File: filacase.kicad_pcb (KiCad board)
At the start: 2 copper layers, 86 x 50 mm, 42 parts, among them J1 Expansion_2, J2 SDcard, J3 SPI 1, J4 Expansion_1, J5 SPI 2, J6 Serial TAG, J7 I2C, J8 +5V, J9 dbg/download port, M3 MountingHole_2.2mm_M2_Pad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

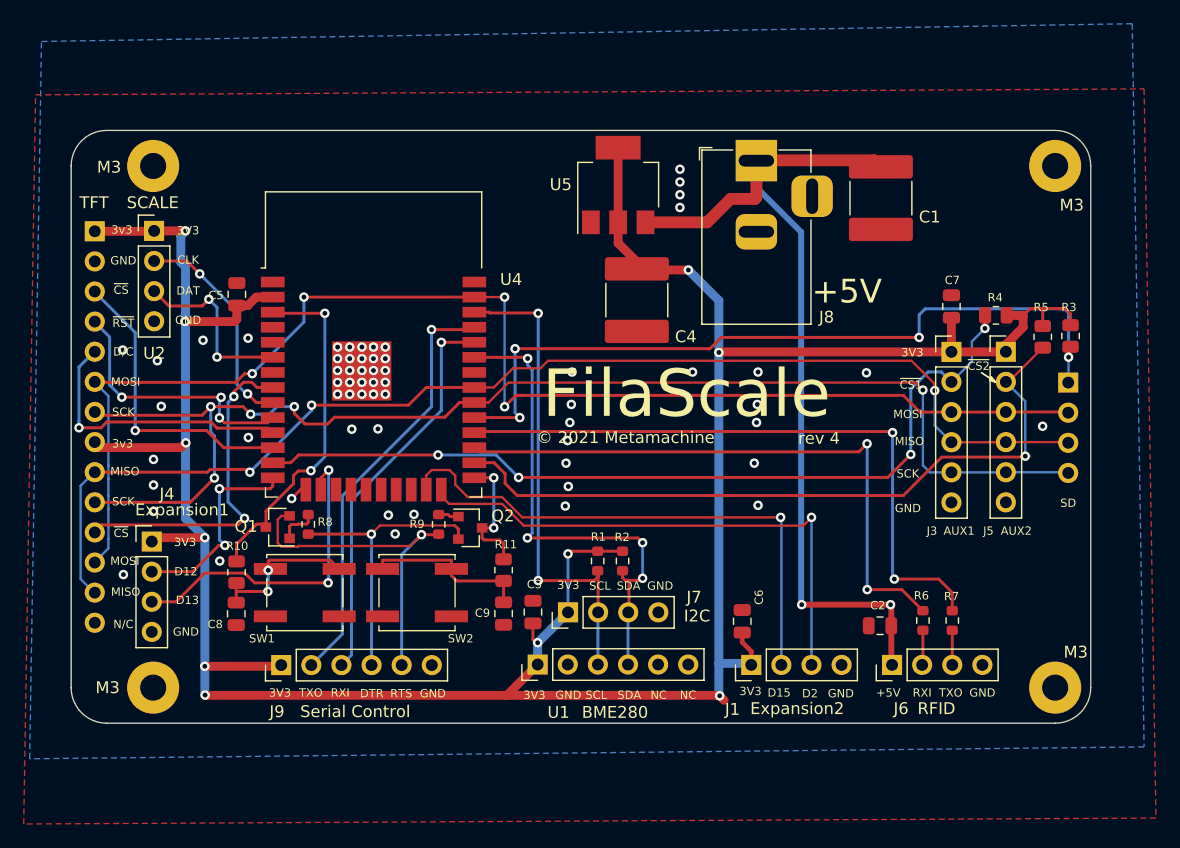
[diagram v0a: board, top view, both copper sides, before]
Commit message: Flip TFT connector around the right way
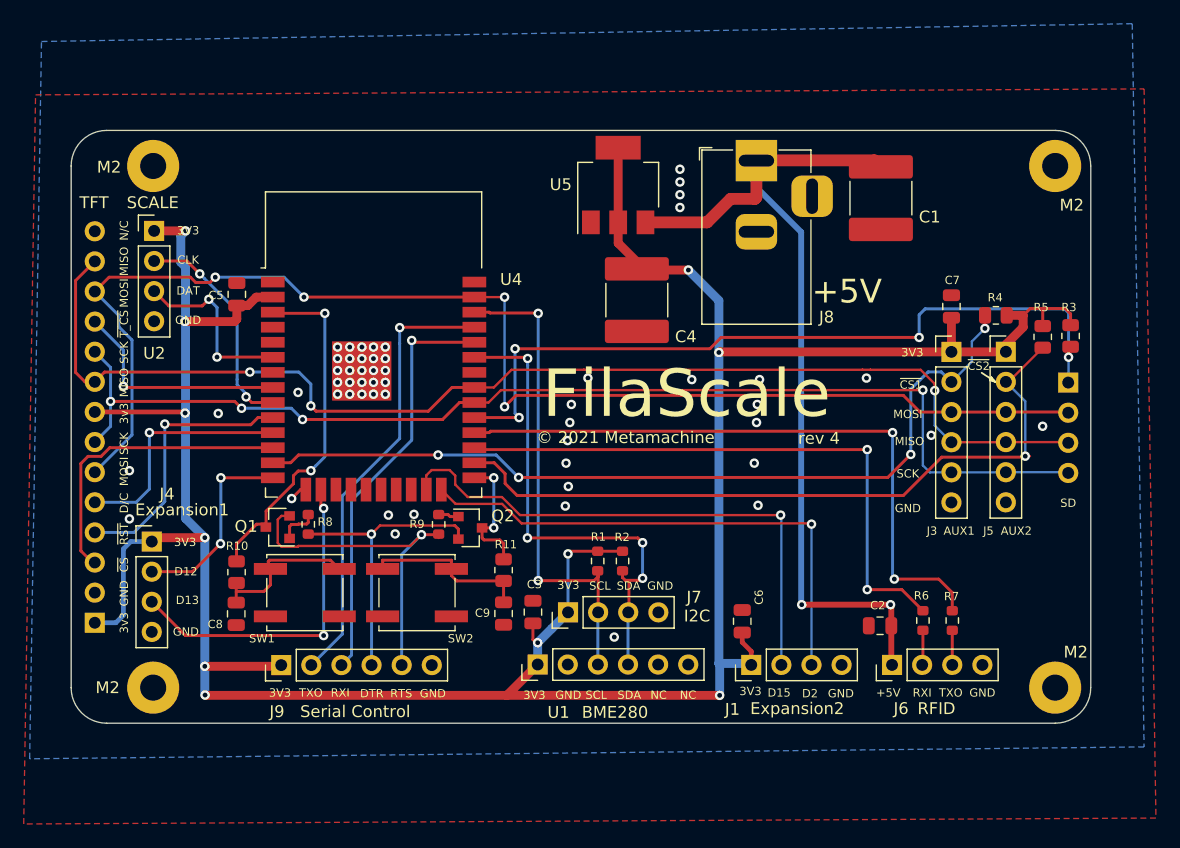
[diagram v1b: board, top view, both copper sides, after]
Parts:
- removed M3 (x2): MountingHole_2.2mm_M2_Pad, MountingHole:MountingHole_2.2mm_M2_Pad
- added M2: MountingHole_2.2mm_M2_Pad, MountingHole:MountingHole_2.2mm_M2_Pad, F.Cu at (64.9, 94.0)
- added M2: MountingHole_2.2mm_M2_Pad, MountingHole:MountingHole_2.2mm_M2_Pad, F.Cu at (141.0, 94.0)
- moved U3 33.0 mm to (60.0, 132.5), turned to 0 degrees
- renumbered M3 to M2
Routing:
- net /SPI_SCK: track 109.5 -> 97.8 mm, vias 5 -> 4
- net /~T_CS~: track 28.4 -> 19.1 mm, vias 2 -> 1
- net +3V3: track 238.2 -> 243.5 mm
- net /TFT_DC: track 23.9 -> 20.2 mm
- net /RX_IN: track 33.5 -> 35.2 mm
- net /TX_OUT: track 36.2 -> 37.9 mm
- net /D2: track 45.5 -> 44.3 mm
- net /SPI_MOSI: track 112.9 -> 111.8 mm
- net /TAG_RX: track 51.3 -> 50.4 mm
- net /D12: track 17.4 -> 16.7 mm
- net /~TFT_RST~: track 22.4 -> 23.0 mm, vias 3 -> 1
- net /~TFT_CS~: track 25.4 -> 25.7 mm, vias 1 -> 0
- net Net-(C8-Pad1): vias 2 -> 0
- net GND: vias 61 -> 54
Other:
- board text added: "~T_CS~"

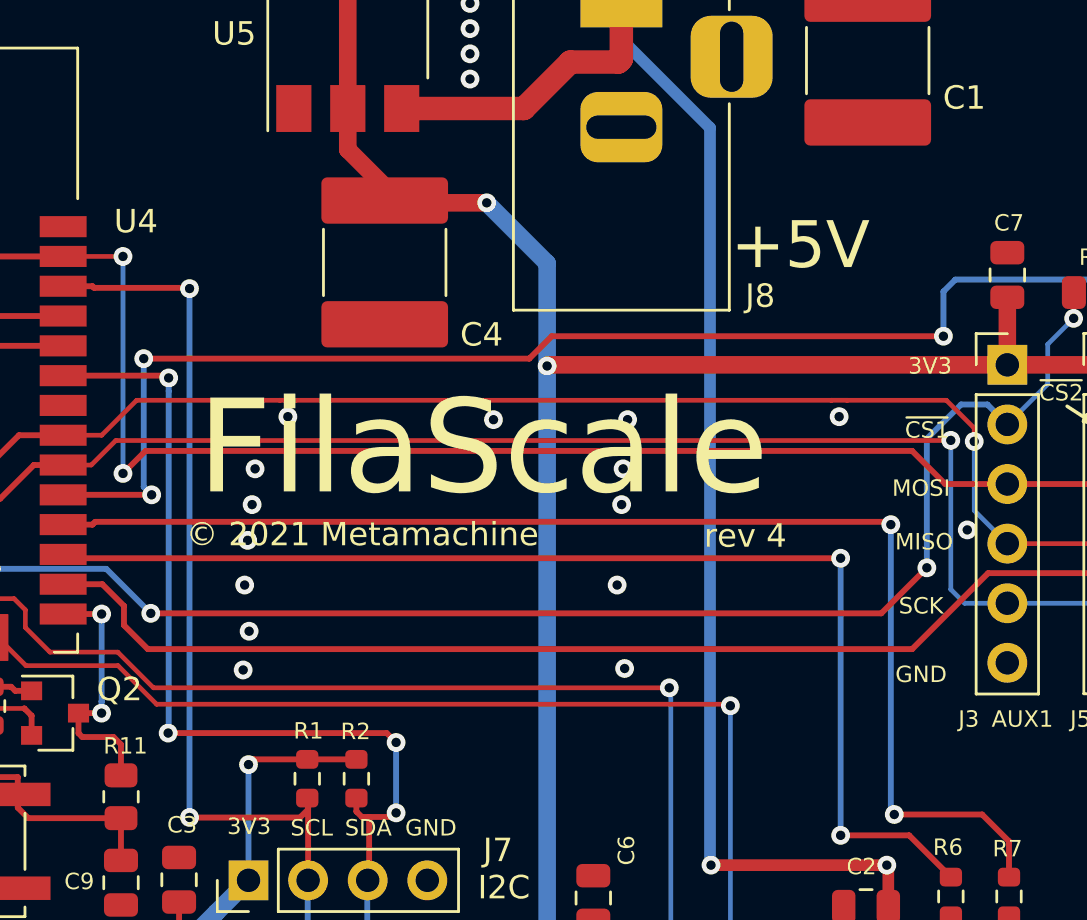
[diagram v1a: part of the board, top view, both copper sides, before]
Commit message: Tweak the layout of a couple of tracks
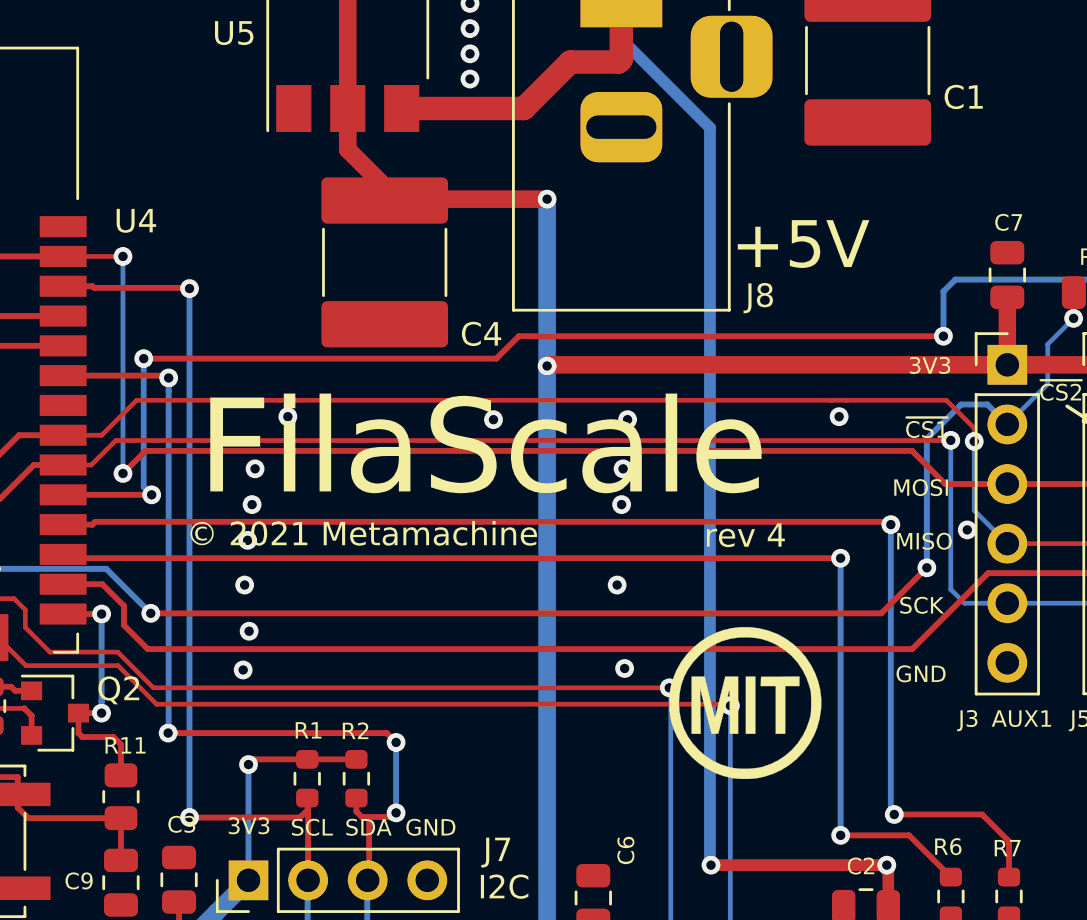
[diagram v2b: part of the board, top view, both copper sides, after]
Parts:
- added G***: LOGO, weo_footprints:MIT_Logo, F.Cu at (121.1, 124.1)
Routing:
- net +3V3: track 243.5 -> 245.1 mm
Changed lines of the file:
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@@
     (thickness 1.6)
     (drawings 85)
-    (tracks 555)
+    (tracks 554)
     (zones 0)
-    (modules 42)
+    (modules 43)
     (nets 50)
   )
@@
     (add_net "Net-(U4-Pad7)")
   )
+  (module weo_footprints:MIT_Logo (layer F.Cu)
+    (at 121.0815 124.0815)
+    (fp_text reference G*** (at 0 0) (layer F.SilkS) hide
+      (effects (font (size 1.524 1.524) (thickness 0.3)))
+    )
+    (fp_text value LOGO (at 0.75 0) (layer F.SilkS) hide
+      (effects (font (size 1.524 1.524) (thickness 0.3)))
+    )
+    (fp_poly (pts (xy 0.189754 -3.220101) (xy 0.581236 -3.173113) (xy 0.963959 -3.080709) (xy 1.331155 -2.943384)
+      (xy 1.400605 -2.911302) (xy 1.739175 -2.722743) (xy 2.049878 -2.495615) (xy 2.330249 -2.234253)
+      (xy 2.577827 -1.942993) (xy 2.790147 -1.626168) (xy 2.964747 -1.288115) (xy 3.099163 -0.93317)
+      (xy 3.190932 -0.565666) (xy 3.237591 -0.189939) (xy 3.236677 0.189675) (xy 3.226842 0.302874)
+      (xy 3.16401 0.700748) (xy 3.062539 1.069577) (xy 2.920238 1.415702) (xy 2.734915 1.745467)
+      (xy 2.720676 1.767485) (xy 2.476291 2.097344) (xy 2.19871 2.389917) (xy 1.890714 2.643367)
+      (xy 1.555087 2.855858) (xy 1.194611 3.025554) (xy 0.812068 3.150616) (xy 0.535274 3.21017)
+      (xy 0.34563 3.233438) (xy 0.125654 3.245624) (xy -0.105404 3.246702) (xy -0.328295 3.236649)
+      (xy -0.523769 3.215437) (xy -0.547697 3.211602) (xy -0.930196 3.121982) (xy -1.297572 2.985883)
+      (xy -1.645622 2.806436) (xy -1.970141 2.586776) (xy -2.266925 2.330034) (xy -2.53177 2.039345)
+      (xy -2.760473 1.71784) (xy -2.908969 1.451919) (xy -3.035932 1.170407) (xy -3.128962 0.899999)
+      (xy -3.191338 0.626325) (xy -3.226335 0.335017) (xy -3.237233 0.0127) (xy -2.825231 0.0127)
+      (xy -2.802632 0.395327) (xy -2.734462 0.755906) (xy -2.620161 1.095751) (xy -2.45917 1.416174)
+      (xy -2.250929 1.718488) (xy -1.99488 2.004007) (xy -1.964323 2.033913) (xy -1.674413 2.280209)
+      (xy -1.360506 2.481731) (xy -1.022594 2.638482) (xy -0.660672 2.750465) (xy -0.5715 2.770418)
+      (xy -0.368461 2.800104) (xy -0.134216 2.813797) (xy 0.114382 2.811974) (xy 0.36048 2.79511)
+      (xy 0.587228 2.763682) (xy 0.723303 2.733831) (xy 1.076518 2.615069) (xy 1.406778 2.452648)
+      (xy 1.710981 2.249672) (xy 1.986025 2.00924) (xy 2.228809 1.734456) (xy 2.43623 1.428422)
+      (xy 2.605187 1.094238) (xy 2.732576 0.735007) (xy 2.736638 0.720608) (xy 2.762186 0.625487)
+      (xy 2.780667 0.543335) (xy 2.793211 0.462724) (xy 2.800949 0.372222) (xy 2.805014 0.260402)
+      (xy 2.806536 0.115832) (xy 2.8067 0.0127) (xy 2.806133 -0.156048) (xy 2.803677 -0.285431)
+      (xy 2.798203 -0.386879) (xy 2.788578 -0.471822) (xy 2.773672 -0.551689) (xy 2.752352 -0.63791)
+      (xy 2.736638 -0.695209) (xy 2.609156 -1.06164) (xy 2.440011 -1.400723) (xy 2.231151 -1.710099)
+      (xy 1.984523 -1.987407) (xy 1.702075 -2.230286) (xy 1.385754 -2.436376) (xy 1.23491 -2.515493)
+      (xy 0.978252 -2.627342) (xy 0.727007 -2.706851) (xy 0.464922 -2.757945) (xy 0.175748 -2.784549)
+      (xy 0.1089 -2.787433) (xy -0.282191 -2.778839) (xy -0.652037 -2.724159) (xy -1.001259 -2.623159)
+      (xy -1.330479 -2.475605) (xy -1.640316 -2.281265) (xy -1.931393 -2.039905) (xy -1.964323 -2.008514)
+      (xy -2.225572 -1.724731) (xy -2.438952 -1.424295) (xy -2.605023 -1.105893) (xy -2.724342 -0.76821)
+      (xy -2.797471 -0.409935) (xy -2.824968 -0.029754) (xy -2.825231 0.0127) (xy -3.237233 0.0127)
+      (xy -3.232483 -0.230688) (xy -3.2166 -0.440344) (xy -3.187129 -0.632591) (xy -3.141616 -0.823749)
+      (xy -3.082774 -1.01476) (xy -2.934783 -1.378837) (xy -2.743139 -1.721167) (xy -2.511704 -2.037966)
+      (xy -2.244342 -2.325453) (xy -1.944917 -2.579845) (xy -1.617292 -2.79736) (xy -1.26533 -2.974215)
+      (xy -0.96956 -3.083654) (xy -0.592412 -3.175864) (xy -0.203718 -3.221182) (xy 0.189754 -3.220101)) (layer F.SilkS) (width 0.01))
+    (fp_poly (pts (xy -1.523208 -0.26035) (xy -1.473791 -0.058189) (xy -1.427855 0.129167) (xy -1.38687 0.295775)
+      (xy -1.352303 0.435691) (xy -1.32562 0.542971) (xy -1.308291 0.611674) (xy -1.302107 0.635)
+      (xy -1.292486 0.625856) (xy -1.274117 0.574783) (xy -1.249335 0.489426) (xy -1.220473 0.377432)
+      (xy -1.209091 0.3302) (xy -1.177253 0.197175) (xy -1.136465 0.028987) (xy -1.090177 -0.160265)
+      (xy -1.041838 -0.356483) (xy -0.994898 -0.545567) (xy -0.990012 -0.56515) (xy -0.852097 -1.1176)
+      (xy -0.3048 -1.1176) (xy -0.3048 1.3208) (xy -0.6604 1.3208) (xy -0.662642 0.34925)
+      (xy -0.6633 0.102858) (xy -0.664151 -0.096591) (xy -0.665384 -0.252954) (xy -0.667193 -0.370089)
+      (xy -0.669768 -0.451852) (xy -0.6733 -0.502102) (xy -0.677981 -0.524695) (xy -0.684003 -0.523488)
+      (xy -0.691557 -0.502338) (xy -0.700834 -0.465104) (xy -0.702653 -0.4572) (xy -0.71822 -0.391908)
+      (xy -0.744503 -0.284832) (xy -0.779642 -0.143408) (xy -0.82178 0.02493) (xy -0.869059 0.212745)
+      (xy -0.91962 0.412602) (xy -0.945456 0.51435) (xy -1.15049 1.3208) (xy -1.439534 1.3208)
+      (xy -1.634458 0.55245) (xy -1.685269 0.351425) (xy -1.73423 0.156357) (xy -1.779315 -0.02459)
+      (xy -1.818502 -0.18325) (xy -1.849767 -0.311459) (xy -1.871087 -0.401051) (xy -1.875223 -0.4191)
+      (xy -1.921066 -0.6223) (xy -1.898018 1.3208) (xy -2.286 1.3208) (xy -2.286 -1.1176)
+      (xy -1.732458 -1.1176) (xy -1.523208 -0.26035)) (layer F.SilkS) (width 0.01))
+    (fp_poly (pts (xy 0.4318 1.3208) (xy 0.0254 1.3208) (xy 0.0254 -1.1176) (xy 0.4318 -1.1176)
+      (xy 0.4318 1.3208)) (layer F.SilkS) (width 0.01))
+    (fp_poly (pts (xy 2.3114 -0.7112) (xy 1.7018 -0.7112) (xy 1.7018 1.3208) (xy 1.2954 1.3208)
+      (xy 1.2954 -0.7112) (xy 0.658263 -0.7112) (xy 0.665681 -0.90805) (xy 0.6731 -1.1049)
+      (xy 2.3114 -1.118304) (xy 2.3114 -0.7112)) (layer F.SilkS) (width 0.01))
+  )
   (module RF_Module:ESP32-WROOM-32 (layer F.Cu)
     (at 83.51 112.045)
@@
   (segment (start 94.75 138.65) (end 69.325002 138.65) (width 0.75) (layer F.Cu) (net 1))
   (segment (start 69.325002 138.65) (end 69.3 138.624998) (width 0.75) (layer F.Cu) (net 1))
-  (via (at 110.062 102.775) (size 0.8) (drill 0.4) (layers F.Cu B.Cu) (net 1))
-  (segment (start 104.14 98.756) (end 104.14 100.506) (width 0.75) (layer F.Cu) (net 1))
-  (segment (start 104.14 100.506) (end 106.409 102.775) (width 0.75) (layer F.Cu) (net 1))
-  (segment (start 106.409 102.775) (end 110.062 102.775) (width 0.75) (layer F.Cu) (net 1))
   (segment (start 115.2395 135.956) (end 115.3665 136.083) (width 0.75) (layer B.Cu) (net 1))
   (segment (start 112.636 135.956) (end 115.2395 135.956) (width 0.75) (layer B.Cu) (net 1))
   (segment (start 132.25 109.68) (end 112.68499 109.68) (width 0.75) (layer F.Cu) (net 1))
   (segment (start 112.636 135.956) (end 112.636 109.72899) (width 0.75) (layer B.Cu) (net 1))
-  (segment (start 110.062 102.775) (end 112.636 105.349) (width 0.75) (layer B.Cu) (net 1))
-  (segment (start 112.636 105.349) (end 112.636 109.72899) (width 0.75) (layer B.Cu) (net 1))
   (segment (start 112.68499 109.68) (end 112.636 109.72899) (width 0.75) (layer F.Cu) (net 1))
   (via (at 112.636 109.72899) (size 0.8) (drill 0.4) (layers F.Cu B.Cu) (net 1))
@@
   (segment (start 67.52449 114.747) (end 67.6145 114.83701) (width 0.4) (layer F.Cu) (net 1))
   (segment (start 59.9945 114.747) (end 67.52449 114.747) (width 0.4) (layer F.Cu) (net 1))
+  (via (at 112.636 102.618499) (size 0.8) (drill 0.4) (layers F.Cu B.Cu) (net 1))
+  (segment (start 112.636 109.72899) (end 112.636 102.618499) (width 0.75) (layer B.Cu) (net 1))
+  (segment (start 104.14 98.756) (end 104.14 100.506) (width 0.75) (layer F.Cu) (net 1))
+  (segment (start 104.14 100.506) (end 106.252499 102.618499) (width 0.75) (layer F.Cu) (net 1))
+  (segment (start 106.252499 102.618499) (end 112.636 102.618499) (width 0.75) (layer F.Cu) (net 1))
   (via (at 62.9155 119.7) (size 0.8) (drill 0.4) (layers F.Cu B.Cu) (net 2))
   (via (at 62.9155 123.764) (size 0.8) (drill 0.4) (layers F.Cu B.Cu) (net 2))
@@
   (segment (start 142.13 110.13) (end 142.13 109.42) (width 0.2) (layer F.Cu) (net 17))
   (via (at 95.443501 109.415) (size 0.8) (drill 0.4) (layers F.Cu B.Cu) (net 17))
-  (segment (start 111.876988 109.415) (end 112.831488 108.4605) (width 0.25) (layer F.Cu) (net 17))
-  (segment (start 95.443501 109.415) (end 111.876988 109.415) (width 0.25) (layer F.Cu) (net 17))
-  (segment (start 112.831488 108.4605) (end 129.527 108.4605) (width 0.25) (layer F.Cu) (net 17))
   (via (at 129.527 108.4605) (size 0.8) (drill 0.4) (layers F.Cu B.Cu) (net 17))
   (segment (start 129.527 108.4605) (end 129.527 106.5555) (width 0.25) (layer B.Cu) (net 17))
@@
   (segment (start 95.443501 109.415) (end 95.443501 114.881511) (width 0.25) (layer B.Cu) (net 17))
   (segment (start 95.443501 114.881511) (end 95.78199 115.22) (width 0.25) (layer B.Cu) (net 17))
+  (segment (start 111.4295 108.4605) (end 129.527 108.4605) (width 0.25) (layer F.Cu) (net 17))
+  (segment (start 110.475 109.415) (end 111.4295 108.4605) (width 0.25) (layer F.Cu) (net 17))
+  (segment (start 95.443501 109.415) (end 110.475 109.415) (width 0.25) (layer F.Cu) (net 17))
   (via (at 127.285 116.49) (size 0.8) (drill 0.4) (layers F.Cu B.Cu) (net 18))
   (via (at 127.4315 128.844) (size 0.8) (drill 0.4) (layers F.Cu B.Cu) (net 18))
